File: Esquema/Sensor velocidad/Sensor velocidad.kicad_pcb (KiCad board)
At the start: 2 copper layers, 0 parts

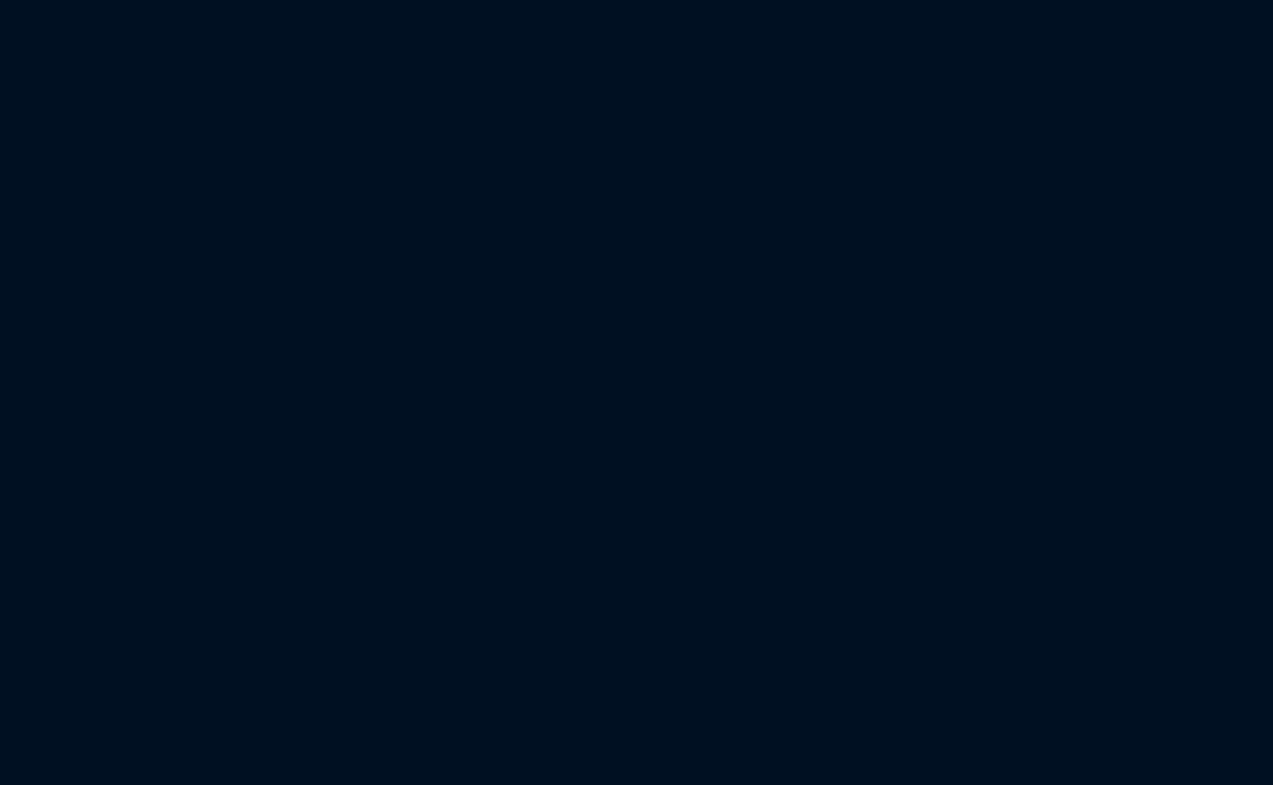
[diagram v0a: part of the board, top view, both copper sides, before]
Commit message: Agregué componentes a proyecto pcb
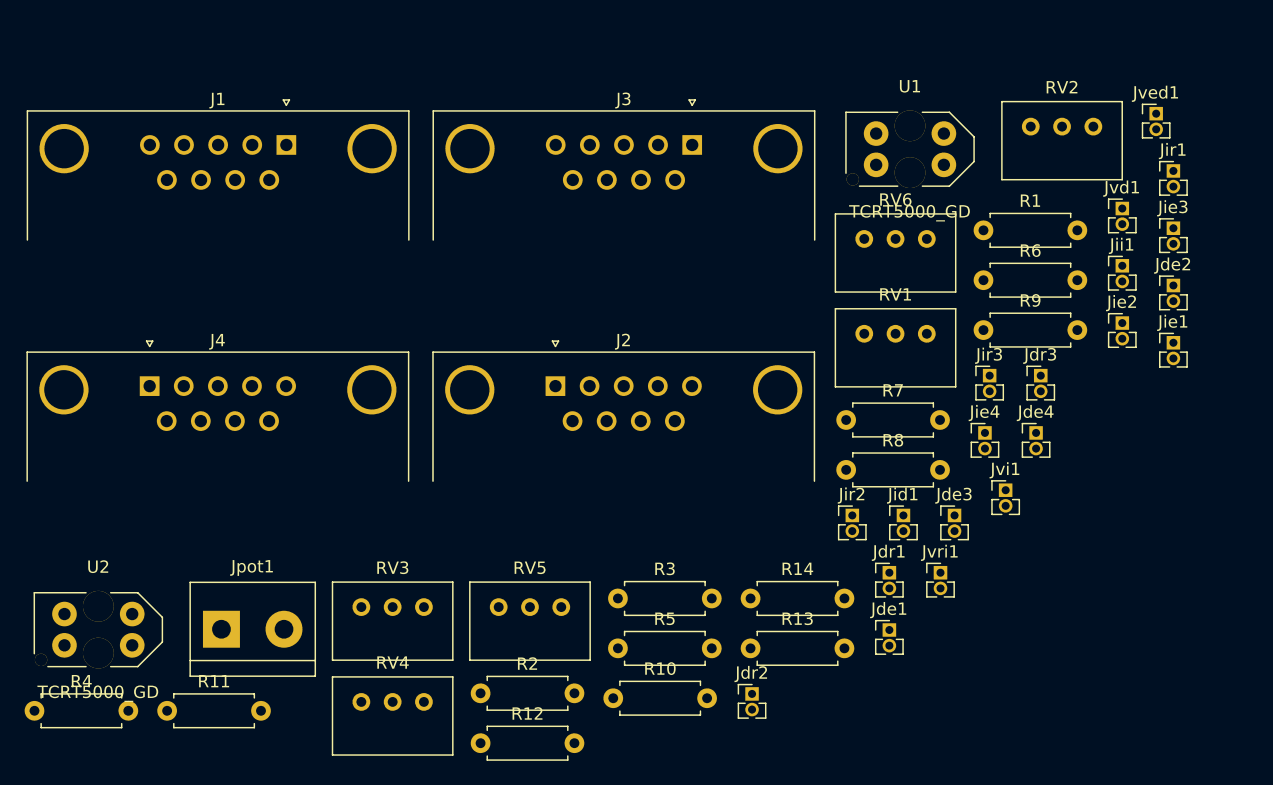
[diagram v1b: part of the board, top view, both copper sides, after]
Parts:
- added J1: DB9_Female_MountingHoles, Connector_Dsub:DSUB-9_Female_Horizontal_P2.77x2.84mm_EdgePinOffset4.94mm_Housed_MountingHolesOffset7.48mm, F.Cu at (93.0, 90.2)
- added J2: DB9_Male_MountingHoles, Connector_Dsub:DSUB-9_Male_Horizontal_P2.77x2.84mm_EdgePinOffset4.94mm_Housed_MountingHolesOffset7.48mm, F.Cu at (114.9, 109.8)
- added J3: DB9_Female_MountingHoles, Connector_Dsub:DSUB-9_Female_Horizontal_P2.77x2.84mm_EdgePinOffset4.94mm_Housed_MountingHolesOffset7.48mm, F.Cu at (126.0, 90.2)
- added J4: DB9_Male_MountingHoles, Connector_Dsub:DSUB-9_Male_Horizontal_P2.77x2.84mm_EdgePinOffset4.94mm_Housed_MountingHolesOffset7.48mm, F.Cu at (81.9, 109.8)
- added Jde1: Jumper_NO_Small, Proy_sen_vel:PinHeader_1x02_P1.27mm_Vertical, F.Cu at (142.0, 129.6)
- added Jde2: Jumper_NO_Small, Proy_sen_vel:PinHeader_1x02_P1.27mm_Vertical, F.Cu at (165.0, 101.6)
- added Jde3: Jumper_NO_Small, Proy_sen_vel:PinHeader_1x02_P1.27mm_Vertical, F.Cu at (147.3, 120.3)
- added Jde4: Jumper_NO_Small, Proy_sen_vel:PinHeader_1x02_P1.27mm_Vertical, F.Cu at (153.9, 113.6)
- added Jdr1: Jumper_NO_Small, Proy_sen_vel:PinHeader_1x02_P1.27mm_Vertical, F.Cu at (142.0, 124.9)
- added Jdr2: Jumper_NO_Small, Proy_sen_vel:PinHeader_1x02_P1.27mm_Vertical, F.Cu at (130.8, 134.8)
- added Jdr3: Jumper_NO_Small, Proy_sen_vel:PinHeader_1x02_P1.27mm_Vertical, F.Cu at (154.3, 108.9)
- added Jid1: Jumper_NO_Small, Proy_sen_vel:PinHeader_1x02_P1.27mm_Vertical, F.Cu at (143.1, 120.3)
- added Jie1: Jumper_NO_Small, Proy_sen_vel:PinHeader_1x02_P1.27mm_Vertical, F.Cu at (165.0, 106.3)
- added Jie2: Jumper_NO_Small, Proy_sen_vel:PinHeader_1x02_P1.27mm_Vertical, F.Cu at (160.9, 104.7)
- added Jie3: Jumper_NO_Small, Proy_sen_vel:PinHeader_1x02_P1.27mm_Vertical, F.Cu at (165.0, 97.0)
- added Jie4: Jumper_NO_Small, Proy_sen_vel:PinHeader_1x02_P1.27mm_Vertical, F.Cu at (149.7, 113.6)
- added Jii1: Jumper_NO_Small, Proy_sen_vel:PinHeader_1x02_P1.27mm_Vertical, F.Cu at (160.9, 100.0)
- added Jir1: Jumper_NO_Small, Proy_sen_vel:PinHeader_1x02_P1.27mm_Vertical, F.Cu at (165.0, 92.3)
- added Jir2: Jumper_NO_Small, Proy_sen_vel:PinHeader_1x02_P1.27mm_Vertical, F.Cu at (139.0, 120.3)
- added Jir3: Jumper_NO_Small, Proy_sen_vel:PinHeader_1x02_P1.27mm_Vertical, F.Cu at (150.1, 108.9)
- added Jpot1: Screw_Terminal_01x02, TerminalBlock:TerminalBlock_bornier-2_P5.08mm, F.Cu at (87.8, 129.5)
- added Jvd1: Conn_01x02_Male, Proy_sen_vel:PinHeader_1x02_P1.27mm_Vertical, F.Cu at (160.9, 95.4)
- added Jved1: Conn_01x02_Male, Proy_sen_vel:PinHeader_1x02_P1.27mm_Vertical, F.Cu at (163.6, 87.7)
- added Jvi1: Conn_01x02_Male, Proy_sen_vel:PinHeader_1x02_P1.27mm_Vertical, F.Cu at (151.4, 118.2)
- added Jvri1: Conn_01x02_Male, Proy_sen_vel:PinHeader_1x02_P1.27mm_Vertical, F.Cu at (146.1, 124.9)
- added R1: 330, Resistor_THT:R_Axial_DIN0207_L6.3mm_D2.5mm_P7.62mm_Horizontal, F.Cu at (149.6, 97.1)
- added R10: 1 K, Resistor_THT:R_Axial_DIN0207_L6.3mm_D2.5mm_P7.62mm_Horizontal, F.Cu at (119.6, 135.1)
- added R11: 10 K, Resistor_THT:R_Axial_DIN0207_L6.3mm_D2.5mm_P7.62mm_Horizontal, F.Cu at (83.3, 136.2)
- added R12: 1 K, Resistor_THT:R_Axial_DIN0207_L6.3mm_D2.5mm_P7.62mm_Horizontal, F.Cu at (108.8, 138.8)
- added R13: 10 K, Resistor_THT:R_Axial_DIN0207_L6.3mm_D2.5mm_P7.62mm_Horizontal, F.Cu at (130.7, 131.1)
- added R14: 100 K, Resistor_THT:R_Axial_DIN0207_L6.3mm_D2.5mm_P7.62mm_Horizontal, F.Cu at (130.7, 127.0)
- added R2: 470, Resistor_THT:R_Axial_DIN0207_L6.3mm_D2.5mm_P7.62mm_Horizontal, F.Cu at (108.8, 134.7)
- added R3: 1 K, Resistor_THT:R_Axial_DIN0207_L6.3mm_D2.5mm_P7.62mm_Horizontal, F.Cu at (119.9, 127.0)
- added R4: 10 K, Resistor_THT:R_Axial_DIN0207_L6.3mm_D2.5mm_P7.62mm_Horizontal, F.Cu at (72.6, 136.2)
- added R5: 1 K, Resistor_THT:R_Axial_DIN0207_L6.3mm_D2.5mm_P7.62mm_Horizontal, F.Cu at (119.9, 131.1)
- added R6: 10 K, Resistor_THT:R_Axial_DIN0207_L6.3mm_D2.5mm_P7.62mm_Horizontal, F.Cu at (149.6, 101.2)
- added R7: 100 K, Resistor_THT:R_Axial_DIN0207_L6.3mm_D2.5mm_P7.62mm_Horizontal, F.Cu at (138.5, 112.5)
- added R8: 330, Resistor_THT:R_Axial_DIN0207_L6.3mm_D2.5mm_P7.62mm_Horizontal, F.Cu at (138.5, 116.6)
- added R9: 470, Resistor_THT:R_Axial_DIN0207_L6.3mm_D2.5mm_P7.62mm_Horizontal, F.Cu at (149.6, 105.2)
- added RV1: 10 K, Potentiometer_THT:Potentiometer_Bourns_3299W_Vertical, F.Cu at (145.0, 105.5)
- added RV2: 100 K, Potentiometer_THT:Potentiometer_Bourns_3299W_Vertical, F.Cu at (158.5, 88.7)
- added RV3: 1 Meg, Potentiometer_THT:Potentiometer_Bourns_3299W_Vertical, F.Cu at (104.2, 127.7)
- added RV4: 10 K, Potentiometer_THT:Potentiometer_Bourns_3299W_Vertical, F.Cu at (104.2, 135.4)
- added RV5: 100 K, Potentiometer_THT:Potentiometer_Bourns_3299W_Vertical, F.Cu at (115.3, 127.7)
- added RV6: 1 Meg, Potentiometer_THT:Potentiometer_Bourns_3299W_Vertical, F.Cu at (145.0, 97.8)
- added U1: TCRT5000_GD, Proy_sen_vel:TCRT5000, F.Cu at (143.7, 90.6)
- added U2: TCRT5000_GD, Proy_sen_vel:TCRT5000, F.Cu at (77.8, 129.6)

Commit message: Modificación de footprints en conectores db para que se vea reflejado en pcb
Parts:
- J1, J3: footprint Connector_Dsub:DSUB-9_Female_Horizontal_P2.77x2.84mm_EdgePinOffset4.94mm_Housed_MountingHolesOffset7.48mm -> Proy_sen_vel:DSUB-9_Female_Horizontal_P2.77x2.84mm_EdgePinOffset4.94mm_Housed_MountingHolesOffset7.48mm
- J2, J4: footprint Connector_Dsub:DSUB-9_Male_Horizontal_P2.77x2.84mm_EdgePinOffset4.94mm_Housed_MountingHolesOffset7.48mm -> Proy_sen_vel:DSUB-9_Male_Horizontal_P2.77x2.84mm_EdgePinOffset4.94mm_Housed_MountingHolesOffset7.48mm

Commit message: Voy acomodando los componentes de la placa, modificar footprint de jumpers porque tienen muy grande los pads
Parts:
- moved Jde1 142.2 mm to (41.5, 29.0)
- moved Jde2 132.1 mm to (49.0, 38.5)
- moved Jde3 129.5 mm to (55.0, 29.5)
- moved RV6 126.6 mm to (33.5, 38.0)
- moved R4 96.7 mm to (62.0, 40.0)
- moved U2 89.4 mm to (147.0, 73.0)
- moved RV3 85.7 mm to (189.5, 136.0)
- moved Jpot1 73.4 mm to (35.5, 78.0), turned to 270 degrees
- moved J2 70.8 mm to (129.5, 40.5), turned to 270 degrees
- moved Jir2 66.6 mm to (205.5, 118.0)
- moved R11 64.2 mm to (59.5, 76.5)
- moved RV4 62.0 mm to (157.0, 168.0)
- moved Jii1 59.1 mm to (219.5, 108.0)
- moved J4 57.5 mm to (129.5, 77.5), turned to 270 degrees
- moved Jvd1 55.0 mm to (215.0, 85.5)
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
